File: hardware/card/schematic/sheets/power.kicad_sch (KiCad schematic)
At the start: 11 parts, among them J1 USB-C-mid, J2 1S-Pouch-403048, U2 BQ24075RGTR, U3 MAX17048G+T10, U4 TPS63070, U6 PanelLoadSwitch, U7 PowerLatch-DNP

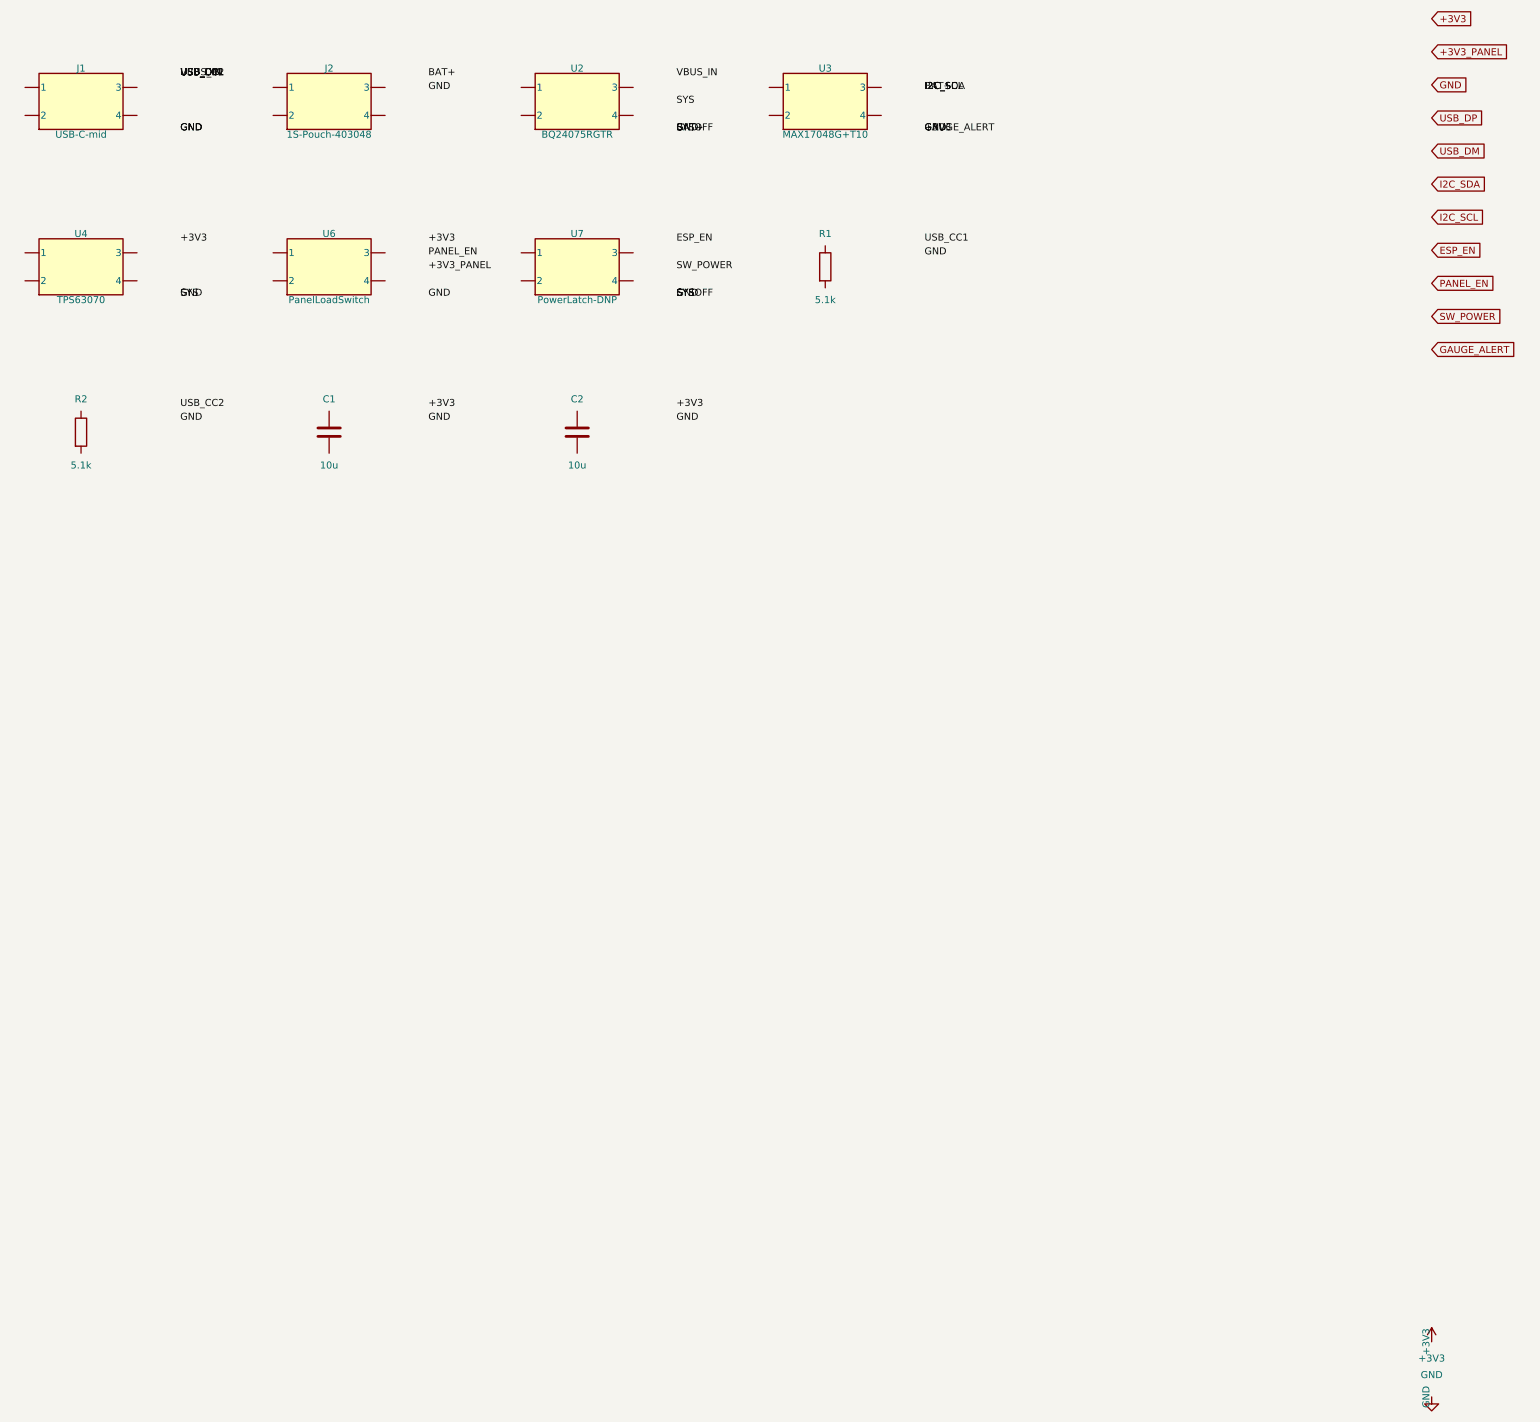
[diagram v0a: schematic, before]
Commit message: hardware: replace U7 power latch with a slide switch (hard off)
Owner-approved power model: top-edge SPDT slide switch gates the TPS63070
EN pin; hard off is the normal off (Game Boy/Arduboy style, ~1-1.5 s tuned
cold boot, end-of-level atomic saves). Deletes the U7 latch IC and SYSOFF
wiring, frees GPIO8, adds a VBUS-powered charge LED on BQ24075 CHG, and
demotes deep sleep to an optional idle battery-saver. Closes the U7
pre-route gate from the 2026-07-09 PCB review.

Co-authored-by: Cursor <cursoragent@cursor.com>
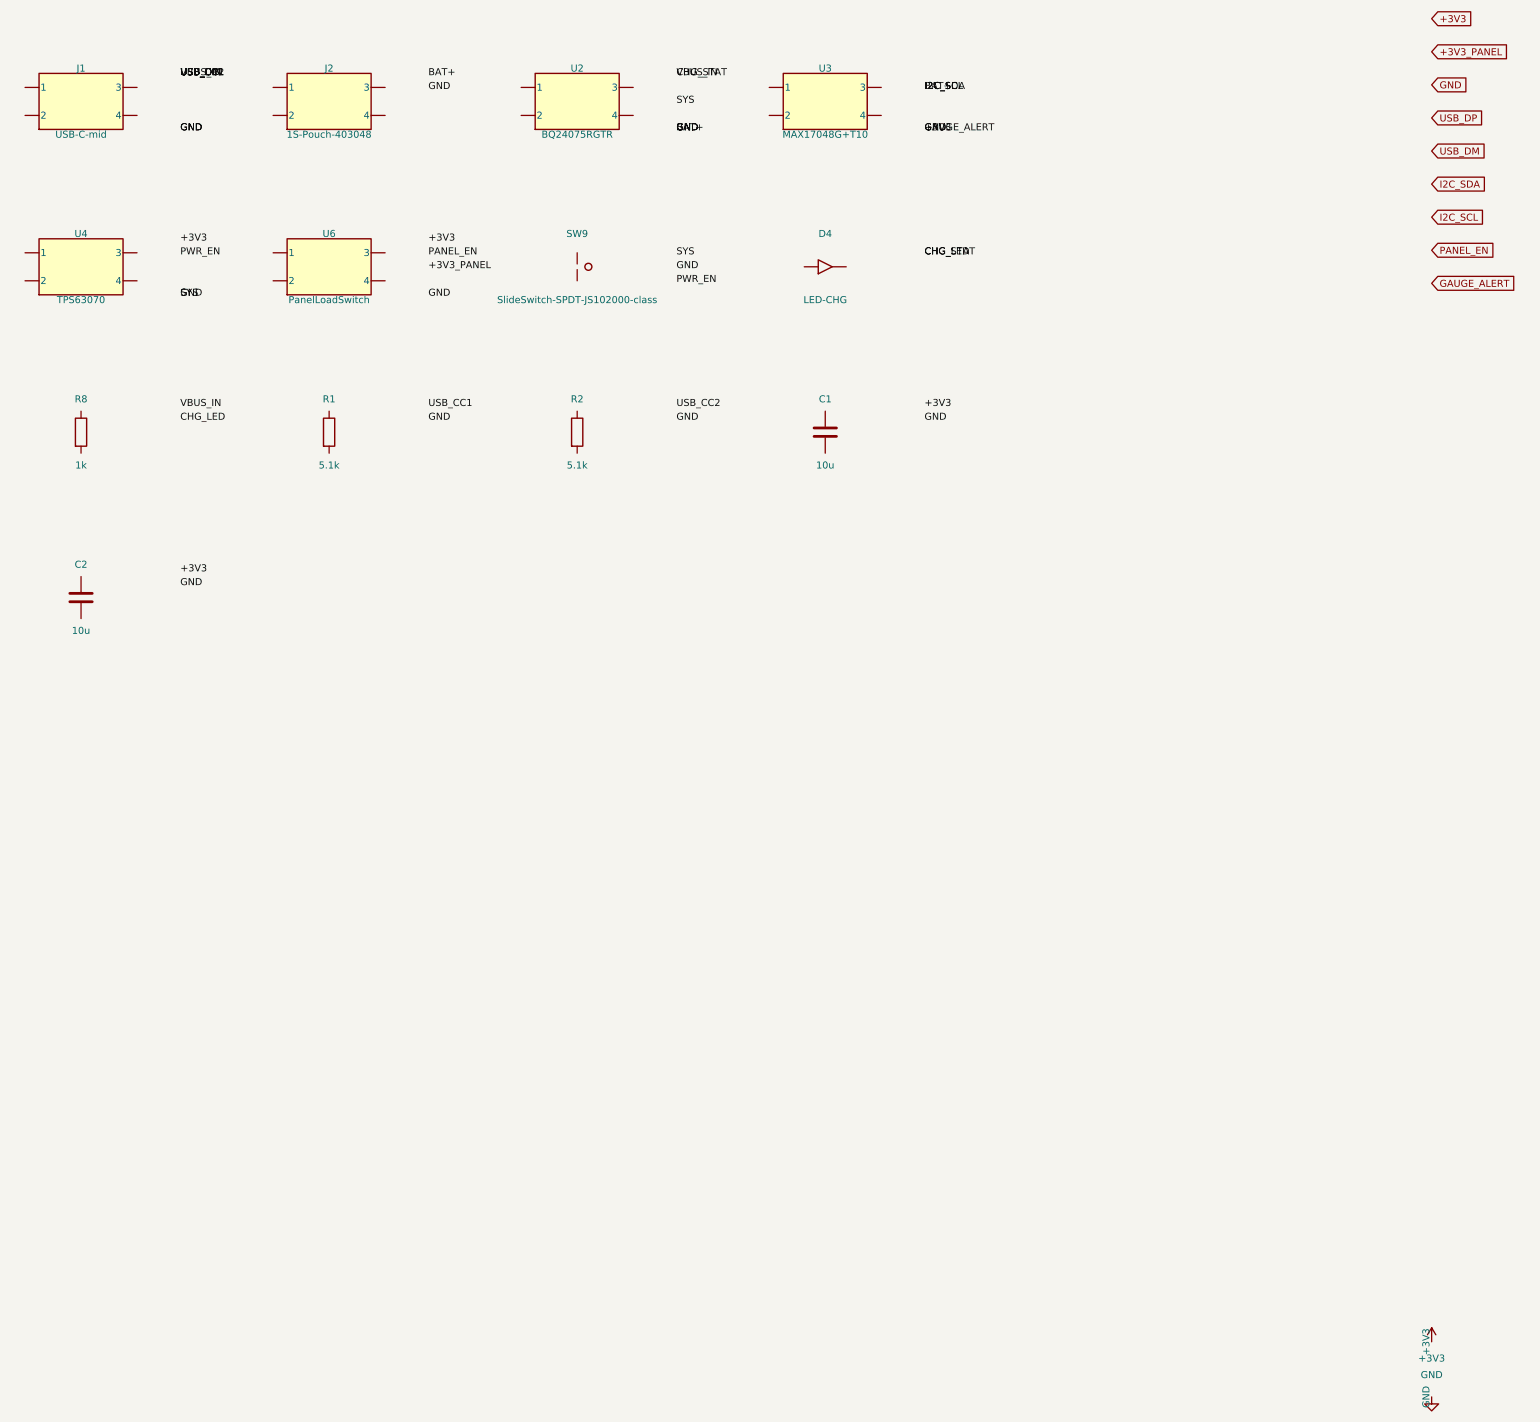
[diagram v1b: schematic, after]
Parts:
- removed U7: PowerLatch-DNP, TBD, symbol PSCard:Block2
- added C1, C2: 10u, 0603, symbol Device:C
- added SW9: SlideSwitch-SPDT-JS102000-class, TBD, symbol Switch:SW_Push
- D4: renamed from R1; value 5.1k -> LED-CHG; footprint 0402 -> 0603; symbol Device:R -> Device:LED
- R1: renamed from C1; value 10u -> 5.1k; footprint 0603 -> 0402; symbol Device:C -> Device:R
- R2: renamed from C2; value 10u -> 5.1k; footprint 0603 -> 0402; symbol Device:C -> Device:R
- R8: renamed from R2; value 5.1k -> 1k

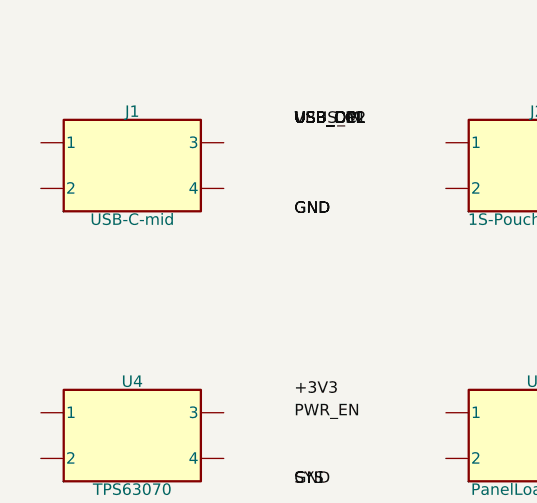
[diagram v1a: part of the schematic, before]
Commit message: hardware: back-mount the USB-C with a rear-shell bump; lock battery requirements
Owner decisions: J1 becomes a standard 16-pin SMD receptacle (TYPE-C-31-M-12
class, JLC basic part) on the PCB back at the top edge, absorbed by a local
~1 mm rear-shell bump (depthProfile.usbBump). This deletes the mid-mount
board notch and the last display-zone Z-stack interaction. Battery is now
specified by requirements (403048 class <=4.3 mm incl. PCM, built-in
protection, wired leads + JST-SH/PH connector) with the exact SKU deferred
to order-time sample measurement.

Co-authored-by: Cursor <cursoragent@cursor.com>
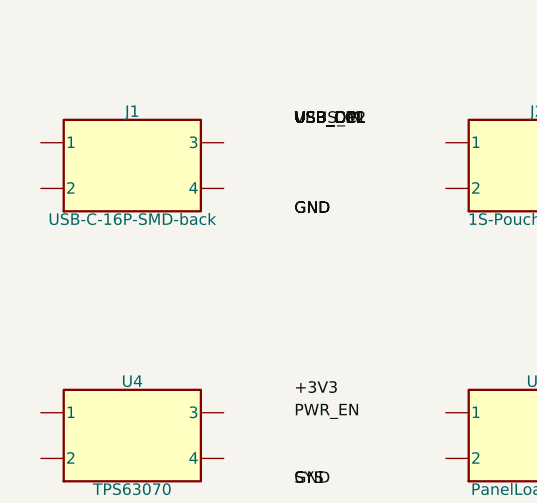
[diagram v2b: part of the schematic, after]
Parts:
- J1: value USB-C-mid -> USB-C-16P-SMD-back; footprint TBD -> TYPE-C-31-M-12-class
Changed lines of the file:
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@@
     (property "Reference" "J1" (at 35 29 0)
       (effects (font (size 1.27 1.27))))
-    (property "Value" "USB-C-mid" (at 35 41 0)
+    (property "Value" "USB-C-16P-SMD-back" (at 35 41 0)
       (effects (font (size 1.27 1.27))))
-    (property "Footprint" "TBD" (at 35 35 0)
+    (property "Footprint" "TYPE-C-31-M-12-class" (at 35 35 0)
       (effects (font (size 1.27 1.27)) hide))
     (property "Datasheet" "~" (at 35 35 0)
